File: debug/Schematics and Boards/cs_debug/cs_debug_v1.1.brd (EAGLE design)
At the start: 83.3 x 62.2 mm, 241 parts, among them J1 J-JTAG-CORTEX_SMD, J19 Solar, J2 J-JTAG-CORTEX_SMD, J3 J-JTAG-CORTEX-NEEDLE6-LEGS, J4 J-SERIAL-PORT, J5 J-WURTH-USBC, Q10 2N7002P, Q3 FDN340P, Q4 2N7002P, Q5 FDN340P, Q6 2N7002P, Q7 FDN340P, Q8 2N7002P, Q9 FDN340P, U1 AP2120N-3.3TRG1, U10 OPA357AIDBVTG4, U11 DAC7574IDGS, U12 MCP73871T-2CCI/ML, U13 USB2412-DZK, U14 INA225AIDGK, U15 OPA357AIDBVTG4, U2 TLV1117LV33DCYR, U5 INA225AIDGK, U6 OPA357AIDBVTG4, U7 INA225AIDGK, U8 OPA357AIDBVTG4, U9 INA225AIDGK, Y1 EPSON_TSX-3225_24.0000MF10Z-C3, Y101 32.768kHz, Y102 12mHz-12pF-K7

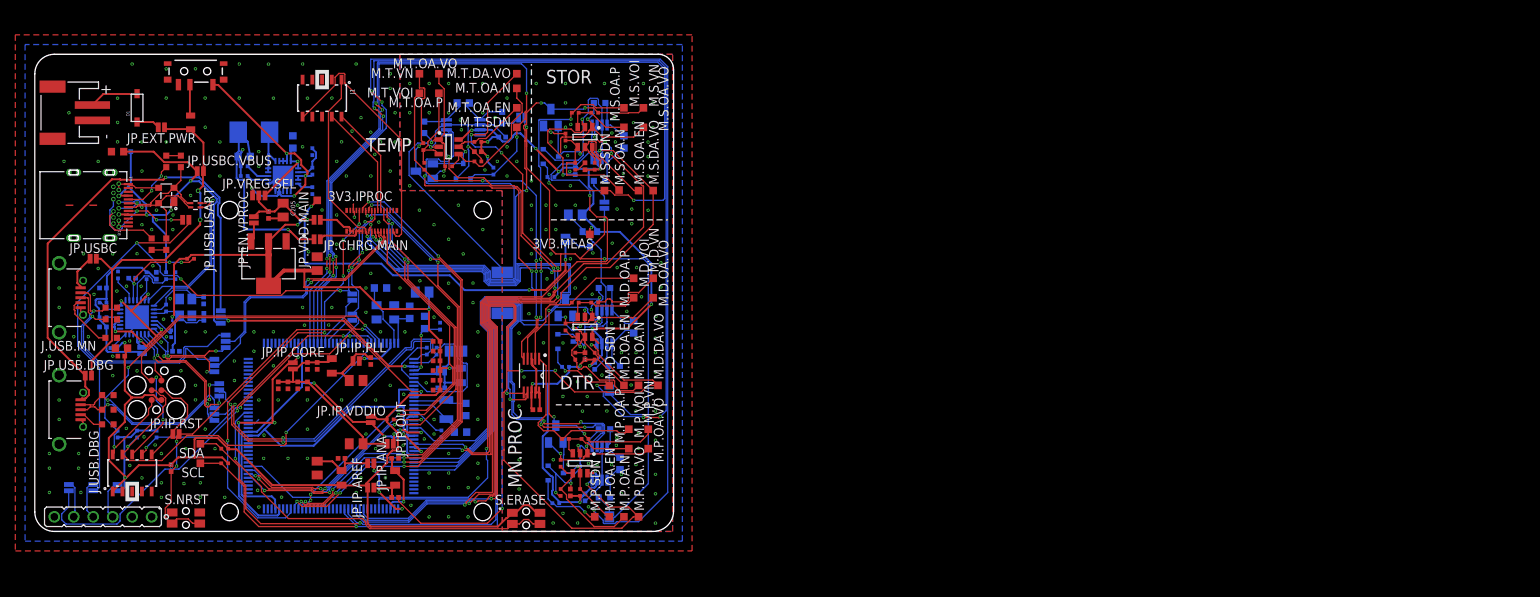
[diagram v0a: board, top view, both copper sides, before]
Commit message: Schematic updates and component placement for debug placement
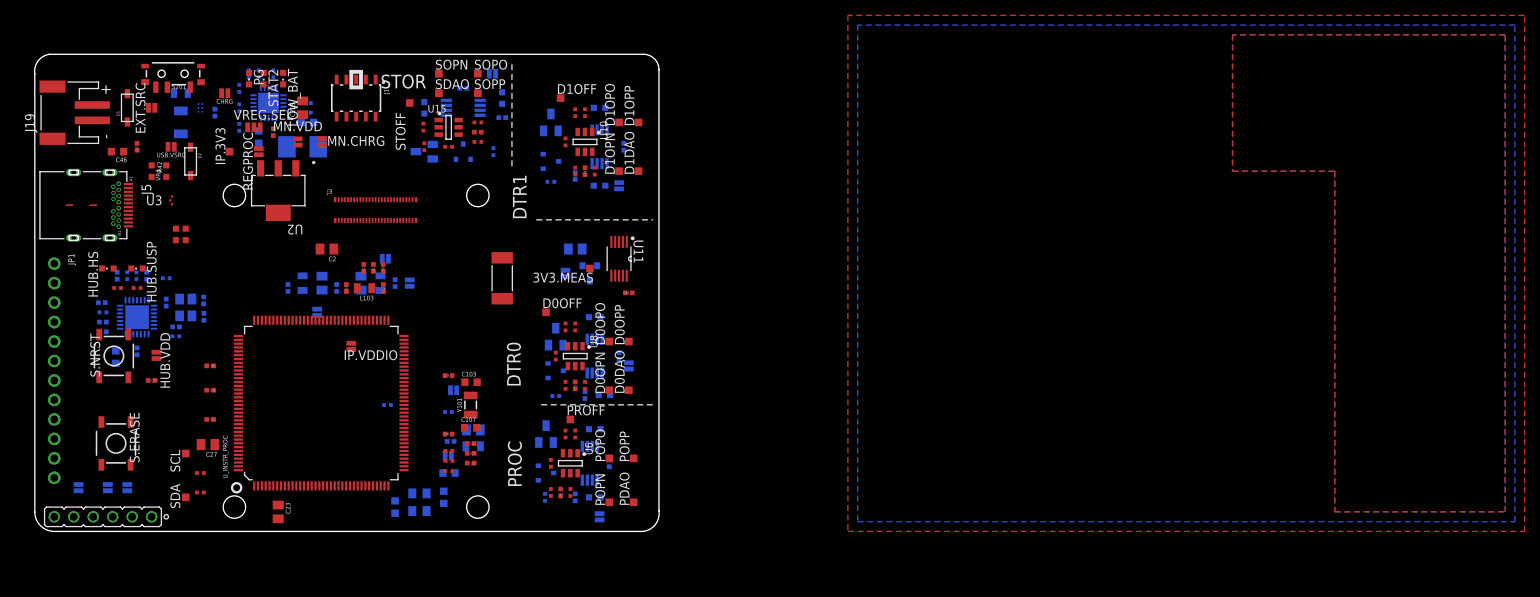
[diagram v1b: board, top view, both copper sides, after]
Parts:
- removed 3V3.IPROC, M.D.DA.VO, M.D.OA.EN, M.D.OA.N, M.D.OA.P, M.D.OA.VO, M.D.SDN, M.D.VN, M.D.VOI, M.P.DA.VO, M.P.OA.EN, M.P.OA.N, M.P.OA.P, M.P.OA.VO, M.P.SDN, M.P.VN, M.P.VOI, M.S.DA.VO, M.S.OA.EN, M.S.OA.N, M.S.OA.P, M.S.OA.VO, M.S.SDN, M.S.VN, M.S.VOI, M.T.DA.VO, M.T.OA.EN, M.T.OA.N, M.T.SDN, M.T.VN, M.T.VOI: TPTP10SQ, TestPoints:TP10SQ
- removed J.USB.DBG, J.USB.MN: USBABSMTDIP, ZX62D-AB-5P8:ZX62D-AB-5P8
- removed J2: J-JTAG-CORTEX_SMD, Connectors:SAMTECH_FTSH-105-01
- removed JP.CHRG.MAIN, JP.EN.VMEAS, JP.EN.VPROC, JP.EXT.PWR, JP.HUB.VDD, JP.IP.ANA, JP.IP.AREF, JP.IP.CORE, JP.IP.OUT, JP.IP.PLL, JP.IP.RST, JP.IP.UTMI, JP.IP.VDDIO, JP.P.DTR, JP.P.PROC, JP.P.STOR, JP.P.TEMP, JP.UART.RX, JP.UART.RX.IP, JP.UART.TX, JP.UART.TX.IP, JP.USB.USART, JP.USBC.VBUS, JP.VDD.MAIN: JUMPER-SMT_2_NC_PASTE_NO-SILK, Connectors:SMT-JUMPER_2_NC_PASTE_NO-SILK
- removed JP.USB.DBG, JP.USBC: JUMPER-SMT_2_NO_PASTEFREE, Connectors:SMT-JUMPER_2_NO_PASTEFREE_NO-SILK
- removed JP.USB.DDN, JP.USB.DDP, JP.USB.MDN, JP.USB.MDP, JP.USB.VBUSP, JP.VREG.SEL: JUMPER-SMT_3_1-NC_PASTE_NO-SILK, Connectors:SMT-JUMPER_3_1-NC_PASTE_NO-SILK
- removed J_DBG_TO_MAIN_HDR: HIROSE-DF40_30-PIN_CONNECTORS-HEADER, Connectors:HRS_DF40C-30DP-0.4V(51)
- removed L2: DLP11SN900HL2L, Inductors:IND_DLP11S_0504_MUR
- removed R44, R45, R51, R52: 10k, Resistors:R0402
- removed R50: 100k, Resistors:R0402
- removed VR1, VR2, VR5, VR6, VR7, VR8: VARISTOR, Diodes:R0603
- added C4, C5, C6: 0.1u, Capacitors:C0402
- added C57: 1u, Capacitors:C0402
- added CHRG, EXT.SRC, HUB.VDD, IP.ANA, IP.AREF, IP.OUT, IP.PLL, IP.UTMI, IP.VDDIO, MN.CHRG, MN.UART.RX, MN.UART.TX, MN.VDD, REGMEAS, REGPROC, USB.VSRC, VP.DTR0, VP.DTR1, VP.PRC, VP.STOR: JUMPER-SMT_2_NC_PASTE_NO-SILK, Connectors:SMT-JUMPER_2_NC_PASTE_NO-SILK
- added D0DAO, D0OFF, D0OPN, D0OPO, D0OPP, D1DAO, D1OFF, D1OPN, D1OPO, D1OPP, PDAO, POPN, POPO, POPP, PROFF, SOPO, SOPP, STOFF: TPSTP10SQ, TestPoints:TP10SQ
- added HUB.HS, HUB.SUSP, LOW_BAT, PG, STAT2: (no value), Diodes:CHIPLED_0603
- added IP.3V3: TPTP10SQ, TestPoints:TP10SQ
- added JP1: (no value), Connectors:1X12_ROUND
- added R10: 270, Resistors:R0402
- added R9: 750, Resistors:R0402
- added U204: LOADSWITCH-MIC94164, Switches:WLCSP6_2X3
- added U3: ESD122DMYR, Diodes:DMY0003A
- added VREG.SEL: JUMPER-SMT_3_1-NC_PASTE_NO-SILK, Connectors:SMT-JUMPER_3_1-NC_PASTE_NO-SILK
- C10, C13, C7: value 270nF -> 0.1u; device Capacitors:C0603 -> Capacitors:C0402
- C20: value 270nF -> 10u; device Capacitors:C0603 -> Capacitors:C1206
- D2: value BGX50A -> MBR120VLSFT3GOSCT-ND; device Diodes:SOT143_BGX50A -> adafruit:SOD-123
- J3: value J-JTAG-CORTEX-NEEDLE6-LEGS -> HIROSE-DF40_50-PIN_CONNECTORS-HEADER; device Connectors:8.06.16_6-PIN_NEEDLE_ADAPTER_LEGS -> Connectors:HRS_DF40C-50DP-0.4V(51)
- JP.UART.VCC: value JUMPER-SMT_2_NC_PASTE_NO-SILK -> JUMPER-SMT_2_NO_PASTEFREE; device Connectors:SMT-JUMPER_2_NC_PASTE_NO-SILK -> Connectors:SMT-JUMPER_2_NO_PASTEFREE_NO-SILK
- R2, R3: value 100k -> 1.5k
- R6: value 100k -> 1.15k
- R7: value 1M -> 100k
- S.ERASE, S.NRST: device Switches:SW_EVQ-P7L01P -> Switches:TACTILE_SWITCH_SMD_5.2MM
- SDAO, SOPN: value TPTP10SQ -> TPSTP10SQ
- Y102: value 12mHz-12pF-K7 -> 12MHz-12pF-K7
- moved S.ERASE 54.4 mm to (-12.3, 11.5), turned to 270 degrees
- moved R2 51.2 mm to (8.26, 59.7), turned to 90 degrees
- moved R3 49.6 mm to (6.35, 59.7), turned to 270 degrees
- moved R6 48.5 mm to (5.08, 59.7)
- moved C10 38.2 mm to (33.0, 57.8), turned to 180 degrees
- moved J3 37.0 mm to (21.6, 41.9), turned to 0 degrees
- moved C20 36.9 mm to (-3.81, 53.3), turned to 270 degrees
- moved C27 34.3 mm to (-0.28, 11.3), flipped to the top, turned to 180 degrees
- moved C17 28.6 mm to (24.1, 3.17), turned to 90 degrees
- moved C22 27.3 mm to (22.6, 31.8), turned to 90 degrees
- moved L101 25.9 mm to (22.2, 32.4), flipped to the bottom, turned to 270 degrees
- moved Y102 25.2 mm to (27.3, 3.81), turned to 270 degrees
- moved L103 25.1 mm to (20.1, 31.7), turned to 180 degrees
- moved C25 24.8 mm to (19.7, 32.4), flipped to the bottom, turned to 90 degrees
- moved C19 24.5 mm to (30.5, 4.45), turned to 270 degrees
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- renumbered M.T.OA.P to SDAO, M.T.OA.VO to SOPN
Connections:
- net CM_DIFFAMP_N2 renamed CM_DTR1_DIFFAMP_N
- net CM_DIFFAMP_P2 renamed CM_DTR1_DIFFAMP_P
- net CM_DTR_DIFFAMP_GAIN0 renamed CM_DTR0_DIFFAMP_GAIN0
- net CM_DTR_DIFFAMP_GAIN1 renamed CM_DTR0_DIFFAMP_GAIN1
- net CM_STORAGE_DIFFAMP_GAIN0 renamed CM_DTR1_DIFFAMP_GAIN0
- net CM_STORAGE_DIFFAMP_GAIN1 renamed CM_DTR1_DIFFAMP_GAIN1
- net CM_TEMP_DIFFAMP_GAIN0 renamed CM_STOR_DIFFAMP_GAIN0
- net CM_TEMP_DIFFAMP_GAIN1 renamed CM_STOR_DIFFAMP_GAIN1
- removed net CM_DIFFAMP_N1: C20.1, R58.2, U14.IN-
- removed net CM_DIFFAMP_N3: C10.1, R31.2, U7.IN-
- removed net CM_DIFFAMP_P1: C20.2, R59.2, U14.IN+
- removed net CM_DIFFAMP_P3: C10.2, R32.2, U7.IN+
- removed net CM_DTR_DCBIAS_SHUTDOWN: M.D.SDN.TP, Q8.G, R30.1, U_INSTR_PROC.15
- removed net CM_DTR_DIFFAMP_OUT: M.D.DA.VO.TP, U7.OUT, U_INSTR_PROC.82
- removed net CM_DTR_V_OFFSET_IN: M.D.VOI.TP, R25.1, U11.2
- removed net CM_DTR_V_SENSE_N: J_DBG_TO_MAIN_HDR.16, M.D.VN.TP, Q7.D, R26.1
- removed net CM_DTR_V_SENSE_P: JP.P.DTR.2, R32.1
- removed net CM_OPAMP_ENABLE1: M.T.OA.EN.TP, Q10.D, Q9.G, R54.1, U15.ENABLE
- removed net CM_OPAMP_ENABLE2: M.S.OA.EN.TP, Q5.G, Q6.D, R34.1, U10.ENABLE
- removed net CM_OPAMP_ENABLE3: M.D.OA.EN.TP, Q7.G, Q8.D, R27.1, U8.ENABLE
- removed net CM_OPAMP_N1: M.T.OA.N.TP, R55.1, R56.2, U15.IN-
- removed net CM_OPAMP_N2: M.S.OA.N.TP, R35.1, R36.2, U10.IN-
- removed net CM_OPAMP_N3: M.D.OA.N.TP, R28.1, R29.2, U8.IN-
- removed net CM_OPAMP_OUT1: Q9.S, R55.2, R58.1, SOPN.TP, U15.OUT
- removed net CM_OPAMP_OUT2: M.S.OA.VO.TP, Q5.S, R35.2, R38.1, U10.OUT
- removed net CM_OPAMP_OUT3: M.D.OA.VO.TP, Q7.S, R28.2, R31.1, U8.OUT
- removed net CM_OPAMP_P2: M.S.OA.P.TP, R24.2, R33.2, U10.IN+
- removed net CM_STORAGE_DCBIAS_SHUTDOWN: M.S.SDN.TP, Q6.G, R37.1, U_INSTR_PROC.14
- removed net CM_STORAGE_DIFFAMP_OUT: M.S.DA.VO.TP, U9.OUT, U_INSTR_PROC.83
- removed net CM_STORAGE_V_OFFSET_IN: M.S.VOI.TP, R24.1, U11.4
- removed net CM_STORAGE_V_SENSE_N: J_DBG_TO_MAIN_HDR.18, M.S.VN.TP, Q5.D, R33.1
- removed net CM_STORAGE_V_SENSE_P: JP.P.STOR.2, R39.1
- removed net CM_TEMP_DCBIAS_SHUTDOWN: M.T.SDN.TP, Q10.G, R57.1, U_INSTR_PROC.13
- removed net CM_TEMP_DIFFAMP_OUT: M.T.DA.VO.TP, U14.OUT, U_INSTR_PROC.84
- removed net CM_TEMP_V_OFFSET_IN: M.T.VOI.TP, R40.1, U11.5
- removed net CM_TEMP_V_SENSE_N: J_DBG_TO_MAIN_HDR.20, M.T.VN.TP, Q9.D, R53.1
- removed net CM_TEMP_V_SENSE_P: JP.P.TEMP.2, R59.1
- removed net HUB_INSTR_PROC_USB_D_N: JP.USB.DDN.3, U13.2
- removed net HUB_INSTR_PROC_USB_D_P: JP.USB.DDP.3, U13.3
- removed net HUB_MAIN_USB_DATA_N: JP.USB.MDN.3, U13.28
- removed net HUB_MAIN_USB_DATA_P: JP.USB.MDP.3, U13.1
- removed net INSTR_PROC_JTAG_TCK/SWCLK: J2.4, J3.4, R3.1, U_INSTR_PROC.28
- removed net INSTR_PROC_JTAG_TDI: J2.8, R6.1, U_INSTR_PROC.29
- removed net INSTR_PROC_JTAG_TDO/SWO: J2.6, J3.6, U_INSTR_PROC.30
- removed net INSTR_PROC_JTAG_TMS/SWDIO: J2.2, J3.2, R2.1, U_INSTR_PROC.31
- removed net INSTR_PROC_NRESET: J2.10, J3.3, JP.IP.RST.1
- removed net MAIN_TRACE_CLK/GPIO4: J_DBG_TO_MAIN_HDR.26, U_INSTR_PROC.97
- removed net MAIN_TRACE_D0/GPIO6: J_DBG_TO_MAIN_HDR.23, U_INSTR_PROC.114
- removed net MAIN_TRACE_D1/GPIO7: J_DBG_TO_MAIN_HDR.25, U_INSTR_PROC.115
- removed net MAIN_TRACE_D2/GPIO8: J_DBG_TO_MAIN_HDR.27
- removed net MAIN_TRACE_D3/GPIO9: J_DBG_TO_MAIN_HDR.29
- removed net MAIN_TRACE_SWO/GPIO5: J_DBG_TO_MAIN_HDR.28, U_INSTR_PROC.113
- removed net USB_BKUP_DBG_D_N: J.USB.DBG.D-, JP.USB.DDN.1, VR5.1
- removed net USB_BKUP_DBG_D_P: J.USB.DBG.D+, JP.USB.DDP.1, VR2.1
- removed net USB_BKUP_DBG_OTGID: J.USB.DBG.USBID, VR1.1
- removed net USB_BKUP_DBG_VBUS: J.USB.DBG.VBUS, JP.USB.DBG.2, JP.USB.VBUSP.1
- removed net USB_BKUP_MAIN_D_N: J.USB.MN.D-, JP.USB.MDP.1, VR8.1
- removed net USB_BKUP_MAIN_D_P: J.USB.MN.D+, JP.USB.MDN.1, VR7.1
- removed net USB_BKUP_MAIN_OTGID: J.USB.MN.USBID, VR6.1
- removed net USB_BKUP_MAIN_VBUS: J.USB.MN.VBUS, JP.USBC.2
- removed net USB_CONN_D_N: D2.2, J5.A6, J5.B6, L2.3, VR3.1
- removed net USB_CONN_D_P: D2.4, J5.A7, J5.B7, L2.2, VR4.1
- removed net VDDOUT_1: JP.IP.CORE.1, U_INSTR_PROC.10, U_INSTR_PROC.104, U_INSTR_PROC.124, U_INSTR_PROC.45, U_INSTR_PROC.61
- new net +3V3_INSTR_PROC: HUB.VDD.1
- new net CM_DTR0_DCBIAS_SHUTDOWN: Q8.G, R30.1, U_INSTR_PROC.15
- new net CM_DTR0_DIFFAMP_N: C7.1, R31.2, U7.IN-
- new net CM_DTR0_DIFFAMP_OUT: D0DAO.TP, U7.OUT, U_INSTR_PROC.82
- new net CM_DTR0_DIFFAMP_P3: C7.2, R32.2, U7.IN+
- new net CM_DTR0_OPAMP_ENABLE: Q7.G, Q8.D, R27.1, U8.ENABLE
- new net CM_DTR0_OPAMP_N: D0OPN.TP, R28.1, R29.2, U8.IN-
- new net CM_DTR0_OPAMP_OUT: D0OPO.TP, Q7.S, R28.2, R31.1, U8.OUT
- new net CM_DTR0_V_OFFSET_IN: D0OFF.TP, R25.1, U11.2
- new net CM_DTR0_V_SENSE_N: J3.18, Q7.D, R26.1
- new net CM_DTR0_V_SENSE_P: R32.1, VP.DTR0.2
- new net CM_DTR1_DCBIAS_SHUTDOWN: Q6.G, R37.1, U_INSTR_PROC.14
- new net CM_DTR1_DIFFAMP_OUT: D1DAO.TP, U9.OUT, U_INSTR_PROC.83
- new net CM_DTR1_OPAMP_N: D1OPN.TP, R35.1, R36.2, U10.IN-
- new net CM_DTR1_OPAMP_OUT: D1OPO.TP, Q5.S, R35.2, R38.1, U10.OUT
- new net CM_DTR1_OPAMP_P: D1OPP.TP, R24.2, R33.2, U10.IN+
- new net CM_DTR1_V_OFFSET_IN: D1OFF.TP, R24.1, U11.4
- new net CM_DTR1_V_SENSE_N: J3.20, Q5.D, R33.1
- new net CM_DTR1_V_SENSE_P: R39.1, VP.DTR1.2
- new net CM_DTR_OPAMP_ENABLE: Q5.G, Q6.D, R34.1, U10.ENABLE
- new net CM_STORV_SENSE_N: J3.22
- new net CM_STOR_DCBIAS_SHUTDOWN: Q10.G, R57.1, U_INSTR_PROC.13
- new net CM_STOR_DIFFAMP_N1: C10.1, R58.2, U14.IN-
- new net CM_STOR_DIFFAMP_OUT: SDAO.TP, U14.OUT, U_INSTR_PROC.84
- new net CM_STOR_DIFFAMP_P1: C10.2, R59.2, U14.IN+
- new net CM_STOR_OPAMP_ENABLE: Q10.D, Q9.G, R54.1, U15.ENABLE
- new net CM_STOR_OPAMP_N: R55.1, R56.2, SOPN.TP, U15.IN-
- new net CM_STOR_OPAMP_OUT: Q9.S, R55.2, R58.1, SOPO.TP, U15.OUT
- new net CM_STOR_V_OFFSET_IN: R40.1, STOFF.TP, U11.5
- new net CM_STOR_V_SENSE_N: Q9.D, R53.1
- new net CM_STOR_V_SENSE_P: R59.1, VP.STOR.2
- new net MAIN_GPIO10: J3.40, U_INSTR_PROC.114
- new net MAIN_GPIO11: J3.38, U_INSTR_PROC.115
- new net MAIN_GPIO4/SERCOM_P0: J3.30, JP1.2
- new net MAIN_GPIO5/SERCOM_P1: J3.32, JP1.3
- new net MAIN_GPIO6/SERCOM_P2: J3.34, JP1.4
- new net MAIN_GPIO7/SERCOM_P3: J3.36, JP1.5
- new net MAIN_GPIO8: J3.44, U_INSTR_PROC.97
- new net MAIN_GPIO9: J3.42, U_INSTR_PROC.113
- new net MAIN_TRACE_CLK/GPIO17: J3.23, JP1.11
- new net MAIN_TRACE_D0/GPIO13: J3.15, JP1.7
- new net MAIN_TRACE_D1/GPIO14: J3.17, JP1.8
- new net MAIN_TRACE_D2/GPIO15: J3.19, JP1.9
- new net MAIN_TRACE_D3/GPIO16: J3.21, JP1.10
- new net MAIN_TRACE_SWO/GPIO12: J3.13, JP1.6
- new net N$12: R2.1, U12.8
- new net N$17: C5.1, U13.25
- new net N$18: R3.2, STAT2.C
- new net N$19: PG.C, R6.2
- new net N$20: R6.1, U12.6
- new net N$22: HUB.SUSP.A, R9.1
- new net N$23: HUB.HS.A, R10.1
- new net N$24: CHRG.1, R201.2, U12.17, U12.18, U12.19, U12.3, U12.4, U12.9
- new net VUSB_DIODE: D2.C, USB.VSRC.1
- net 3V3_INSTR_MEAS: now also JP1.1
- net 3V3_INSTR_PROC: now also IP.3V3.TP, IP.AREF.1, IP.VDDIO.2, S.ERASE.1; no longer 3V3.IPROC.TP, C49.1, C50.1, C51.1, C52.1, C53.1, C54.1, J2.1, J3.1, JP.HUB.VDD.1, JP.IP.AREF.1, JP.IP.VDDIO.2, R2.2, R3.2, R44.2, R45.2, R51.2, R52.2, R6.2, S.ERASE.1_1, S.ERASE.1_2
- net ADVREF_PRE: now also IP.AREF.2; no longer JP.IP.AREF.2
- net CM_DIFFAMP_N4: now also C6.1; no longer C7.1
- net CM_DIFFAMP_P4: now also C6.2; no longer C7.2
- net CM_OPAMP_ENABLE4: no longer M.P.OA.EN.TP
- net CM_OPAMP_N4: now also POPN.TP; no longer M.P.OA.N.TP
- net CM_OPAMP_OUT4: now also POPO.TP; no longer M.P.OA.VO.TP
- net CM_OPAMP_P1: now also SOPP.TP; no longer SDAO.TP
- net CM_OPAMP_P3: now also D0OPP.TP; no longer M.D.OA.P.TP
- net CM_OPAMP_P4: now also POPP.TP; no longer M.P.OA.P.TP
- net CM_PROC_DCBIAS_SHUTDOWN: no longer M.P.SDN.TP
- net CM_PROC_DIFFAMP_OUT: now also PDAO.TP; no longer M.P.DA.VO.TP
- net CM_PROC_V_OFFSET_IN: now also PROFF.TP; no longer M.P.VOI.TP
- net CM_PROC_V_SENSE_N: now also J3.16; no longer J_DBG_TO_MAIN_HDR.14, M.P.VN.TP
- net CM_PROC_V_SENSE_P: now also VP.PRC.2; no longer JP.P.PROC.2
- net DGND: now also C20.2, C4.2, C5.2, C57.2, HUB.HS.C, HUB.SUSP.C, J3.1, J3.3, J3.7, JP1.12, R7.1, S.NRST.1, U204.C1, U3.1; no longer D2.3, J.USB.DBG.GND, J.USB.DBG.S1, J.USB.DBG.S2, J.USB.DBG.S3, J.USB.DBG.S4, J.USB.MN.GND, J.USB.MN.S1, J.USB.MN.S2, J.USB.MN.S3, J.USB.MN.S4, J2.3, J2.5, J2.9, J_DBG_TO_MAIN_HDR.1, J_DBG_TO_MAIN_HDR.3, J_DBG_TO_MAIN_HDR.5, R50.1, S.NRST.1_1, S.NRST.1_2, VR1.2, VR2.2, VR5.2, VR6.2, VR7.2, VR8.2
- net ERASE_S: now also S.ERASE.3; no longer S.ERASE.2_1, S.ERASE.2_2
- net INSTR_PROC_NRESET_SW: now also S.NRST.3; no longer JP.IP.RST.2, S.NRST.2_1, S.NRST.2_2
- net INSTR_PROC_USB_D_N: now also U13.28; no longer JP.USB.DDN.2
- net INSTR_PROC_USB_D_P: now also U13.1; no longer JP.USB.DDP.2
- net MAIN_GPIO0: now also J3.31; no longer J_DBG_TO_MAIN_HDR.7
- net MAIN_GPIO1: now also J3.29; no longer J_DBG_TO_MAIN_HDR.9
- net MAIN_GPIO2: now also J3.27; no longer J_DBG_TO_MAIN_HDR.11
- net MAIN_GPIO3: now also J3.25; no longer J_DBG_TO_MAIN_HDR.13
- net MAIN_NRESET: now also J3.24; no longer J_DBG_TO_MAIN_HDR.30
- net MAIN_SWD_SWCLK: now also J3.28; no longer J_DBG_TO_MAIN_HDR.19
- net MAIN_SWD_SWDIO: now also J3.26; no longer J_DBG_TO_MAIN_HDR.21
- net MAIN_USART_RX: now also J3.9, MN.UART.RX.1; no longer JP.UART.RX.1, JP.UART.TX.IP.1, J_DBG_TO_MAIN_HDR.17
- net MAIN_USART_TX: now also J3.11, MN.UART.TX.1; no longer JP.UART.RX.IP.1, JP.UART.TX.1, JP.USB.USART.2, J_DBG_TO_MAIN_HDR.15
- net MAIN_USB_DATA_N: now also J3.49, U13.2; no longer JP.USB.MDN.2, J_DBG_TO_MAIN_HDR.22
- net MAIN_USB_DATA_P: now also J3.47, U13.3; no longer JP.USB.MDP.2, J_DBG_TO_MAIN_HDR.24
- net N$1: now also REGMEAS.2; no longer JP.EN.VMEAS.2
- net N$14: now also R3.1, U12.7; no longer R45.1, U13.7
- net N$15: now also EXT.SRC.1; no longer JP.EXT.PWR.1
- net N$16: now also C4.1, U13.9; no longer R44.1, U13.11
- net N$3: now also S201.2, U204.C2; no longer JP.UART.TX.IP.2, U_INSTR_PROC.18
- net N$4: now also REGPROC.2; no longer JP.EN.VPROC.2
- net N$5: now also LOW_BAT.C, R2.2; no longer JP.UART.RX.IP.2, U_INSTR_PROC.17
- net N$6: now also C20.1, S201.3, U204.A2, U204.B2; no longer S201.2
- net N$7: now also MN.UART.TX.2; no longer JP.UART.TX.2
- net N$9: now also MN.UART.RX.2; no longer JP.UART.RX.2
- net UCTX_DBGRX: no longer JP.USB.USART.1
- net USBC_VBUS: now also D2.A; no longer D2.1, JP.USB.VBUSP.3, JP.USBC.VBUS.1
- net USB_D_N: now also J5.A7, J5.B7, U3.2, VR3.1; no longer L2.4
- net USB_D_P: now also J5.A6, J5.B6, U3.3, VR4.1; no longer L2.1
- net USB_HS_IND: now also R10.2; no longer R50.2
- net USB_HUB_VDD: now also C49.1, C50.1, C51.1, C52.1, C53.1, C54.1, HUB.VDD.2; no longer JP.HUB.VDD.2
- net USB_NONRMV0: now also R9.2; no longer R51.1
- net USB_NONRMV1: now also R7.2; no longer R52.1
- net USB_VBUS_IPROC: no longer JP.USB.VBUSP.2
- net USB_XIN: no longer R7.2
- net USB_XOUT: no longer R7.1
- net VCHRG_BATT: now also MN.CHRG.1; no longer JP.CHRG.MAIN.1
- net VCHRG_OUT: now also VREG.SEL.3; no longer JP.VREG.SEL.3
- net VDDANA1: now also IP.ANA.2; no longer JP.IP.ANA.2
- net VDDANA_0: now also IP.ANA.1; no longer JP.IP.ANA.1
- net VDDIO1: now also IP.VDDIO.1; no longer JP.IP.VDDIO.1
- net VDDOUT: now also IP.OUT.2, U_INSTR_PROC.10, U_INSTR_PROC.104, U_INSTR_PROC.124, U_INSTR_PROC.45, U_INSTR_PROC.61; no longer JP.IP.CORE.2, JP.IP.OUT.2
- net VDDOUTMI: now also IP.UTMI.2; no longer JP.IP.UTMI.2
- net VDDOUTMI_0: now also IP.UTMI.1; no longer JP.IP.UTMI.1
- net VDDOUT_0: now also IP.OUT.1; no longer JP.IP.OUT.1
- net VDDPLL: now also IP.PLL.2; no longer JP.IP.PLL.2
- net VDDPLL_0: now also IP.PLL.1; no longer JP.IP.PLL.1
- net VDD_TO_MAIN: now also J3.2, J3.4, J3.6, MN.VDD.2; no longer JP.VDD.MAIN.2, J_DBG_TO_MAIN_HDR.2, J_DBG_TO_MAIN_HDR.4
- net VREG_IN: now also MN.VDD.1, REGMEAS.1, REGPROC.1, VREG.SEL.2; no longer JP.EN.VMEAS.1, JP.EN.VPROC.1, JP.VDD.MAIN.1, JP.VREG.SEL.2
- net VSRC: now also EXT.SRC.2, USB.VSRC.2; no longer JP.EXT.PWR.2, JP.USB.DBG.1, JP.USBC.1, JP.USBC.VBUS.2
- net VSRC_RAW: now also C57.1, CHRG.2, LOW_BAT.A, PG.A, STAT2.A, U204.A1, U204.B1, VREG.SEL.1; no longer JP.VREG.SEL.1, R201.2, S201.3, U12.17, U12.18, U12.19, U12.3, U12.4, U12.9
- net V_BATT_MAIN: now also J3.10, J3.12, J3.8, MN.CHRG.2; no longer JP.CHRG.MAIN.2, J_DBG_TO_MAIN_HDR.10, J_DBG_TO_MAIN_HDR.6, J_DBG_TO_MAIN_HDR.8
- net V_SENSE_P: now also J3.14, VP.DTR0.1, VP.DTR1.1, VP.PRC.1, VP.STOR.1; no longer JP.P.DTR.1, JP.P.PROC.1, JP.P.STOR.1, JP.P.TEMP.1, J_DBG_TO_MAIN_HDR.12
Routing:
- net 3V3_INSTR_PROC: track 245.0 -> 0.00 mm, vias 7 -> 0
- net AGND: track 160.7 -> 0.00 mm, vias 127 -> 0
- net CM_PROC_DCBIAS_SHUTDOWN: track 159.5 -> 0.00 mm, vias 6 -> 0
- net CM_DTR_DCBIAS_SHUTDOWN: track 147.7 -> 0.00 mm, vias 8 -> 0
- net V_SENSE_P: track 140.3 -> 0.00 mm, vias 5 -> 0
- net 3V3_INSTR_MEAS: track 123.0 -> 0.00 mm, vias 14 -> 0
- net CM_STORAGE_DCBIAS_SHUTDOWN: track 114.7 -> 0.00 mm, vias 6 -> 0
- net CM_DTR1_DIFFAMP_GAIN0: track 103.0 -> 0.00 mm, vias 2 -> 0
- net CM_PROC_DIFFAMP_OUT: track 97.1 -> 0.00 mm, vias 2 -> 0
- net INSTR_PROC_I2C_SDA: track 96.4 -> 0.00 mm, vias 2 -> 0
- net CM_TEMP_DIFFAMP_OUT: track 95.8 -> 0.00 mm, vias 5 -> 0
- net INSTR_PROC_I2C_SCL: track 93.3 -> 0.00 mm, vias 2 -> 0
- net CM_DTR_DIFFAMP_OUT: track 90.7 -> 0.00 mm, vias 4 -> 0
- net MAIN_USART_TX: track 89.2 -> 0.00 mm, vias 6 -> 0
- net CM_STORAGE_DIFFAMP_OUT: track 87.0 -> 0.00 mm, vias 2 -> 0
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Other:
- board size 83.3 x 62.2 mm -> 81.5 x 62.2 mm
- board text added: "DTR0"
- board text added: "DTR1"
- board text added: "PROC"
- board text removed: "DTR"
- board text removed: "MN.PROC"
- board text removed: "TEMP"

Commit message: Finished schematic revision for main, debug boards.
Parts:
- C.PHAT: value 10u -> 47u
- moved IP.VDDIO 13.7 mm to (6.99, 31.8), flipped to the bottom, turned to 90 degrees
- moved C2 11.9 mm to (3.81, 40.0), turned to 270 degrees
- moved R41 7.97 mm to (31.1, 16.0), flipped to the top, turned to 0 degrees
- moved D1OFF 1.91 mm to (43.8, 56.5)
- moved STOFF 1.91 mm to (26.0, 54.0)
- moved SDAO 1.90 mm to (27.9, 57.1)
- moved SOPN 1.90 mm to (27.9, 59.7)
- moved C16 1.27 mm to (55.9, 31.1)
- moved D0OPO 1.27 mm to (52.1, 26.0)
- moved D0OPP 1.27 mm to (54.6, 26.0)
- moved POPO 1.27 mm to (52.1, 10.8)
- moved POPP 1.27 mm to (55.2, 10.8)
- moved D1OPO 1.27 mm to (53.3, 54.6)
- moved D1OPP 1.27 mm to (55.9, 54.6)
- moved IP.PLL 0.90 mm to (14.6, 29.2)
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- renumbered C20 to C.PHAT, J4 to J.FTDI, R1 to R.GND, U_INSTR_PROC to U.IP
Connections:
- net N$3 renamed VREG.SW.EN
- net N$6 renamed VSRC_SW
- removed net USB_VBUS_IPROC: U.IP.39
- net USBC_VBUS: now also U.IP.39
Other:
- board text added: "GPIO_MAIN"

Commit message: Route differential USB signals
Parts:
- added R1: 51k, Resistors:R0402
- moved VR4 5.72 mm to (-2.54, 44.5), turned to 0 degrees
- moved VR3 5.46 mm to (-2.54, 42.5), turned to 0 degrees
- moved C39 1.19 mm to (34.0, 7.72)
- moved C37 0.99 mm to (34.0, 9.19)
- moved C38 0.92 mm to (34.0, 10.5)
- moved C52 0.36 mm to (-5.66, 30.2)
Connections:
- removed net N$22: HUB.SUSP.A, R9.1
- new net N$3: HUB.SUSP.C, R9.1
- net 3V3_INSTR_PROC: now also HUB.SUSP.A, R1.1
- net DGND: no longer HUB.SUSP.C
- net USB_NONRMV0: now also R1.2
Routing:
- net MAIN_USB_DATA_N: track 0.00 -> 58.5 mm, vias 0 -> 3
- net MAIN_USB_DATA_P: track 0.00 -> 58.3 mm, vias 0 -> 3
- net INSTR_PROC_USB_D_P: track 0.00 -> 54.1 mm, vias 0 -> 1
- net INSTR_PROC_USB_D_N: track 0.00 -> 53.6 mm, vias 0 -> 1
- net USB_D_P: track 0.00 -> 30.9 mm, vias 0 -> 2
- net USB_D_N: track 0.00 -> 27.8 mm, vias 0 -> 2
- net USB_XOUT: track 0.00 -> 8.94 mm
- net USB_XIN: track 0.00 -> 7.15 mm

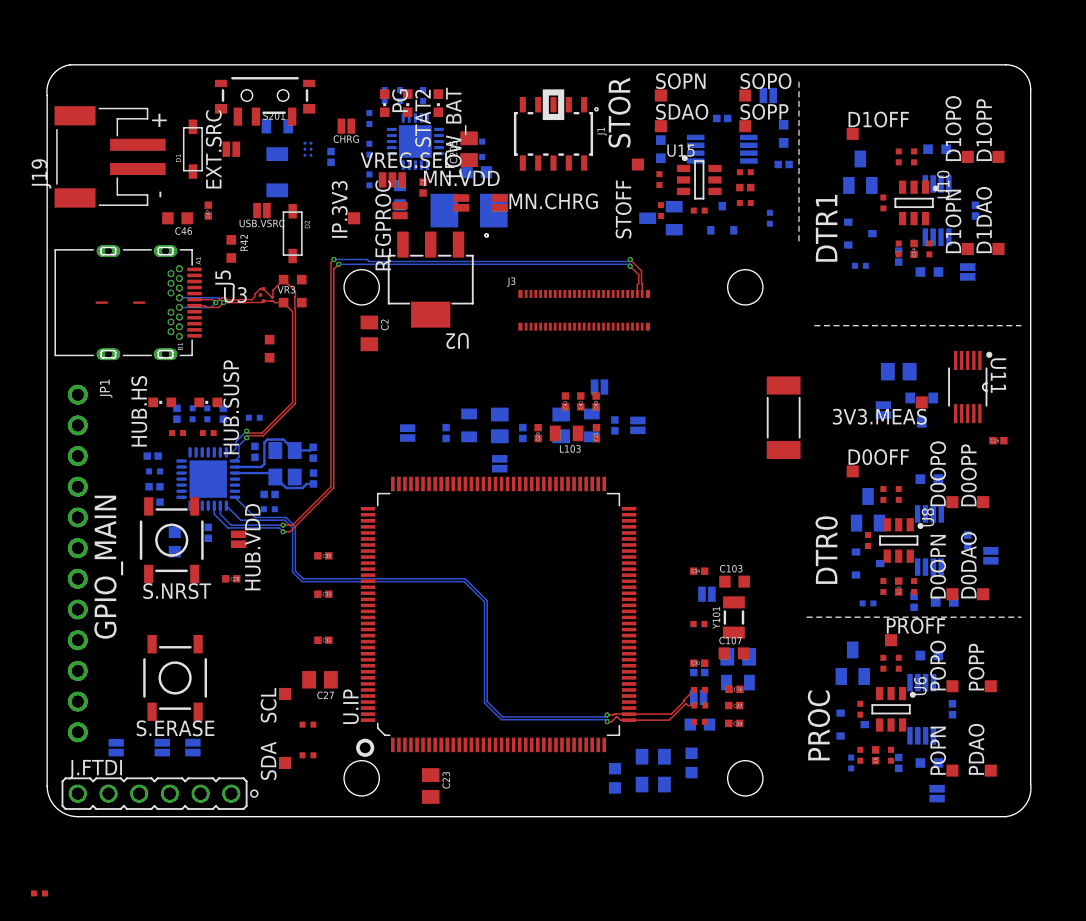
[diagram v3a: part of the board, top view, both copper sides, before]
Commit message: Edit silk and documentation layers for pick-and-place assembly
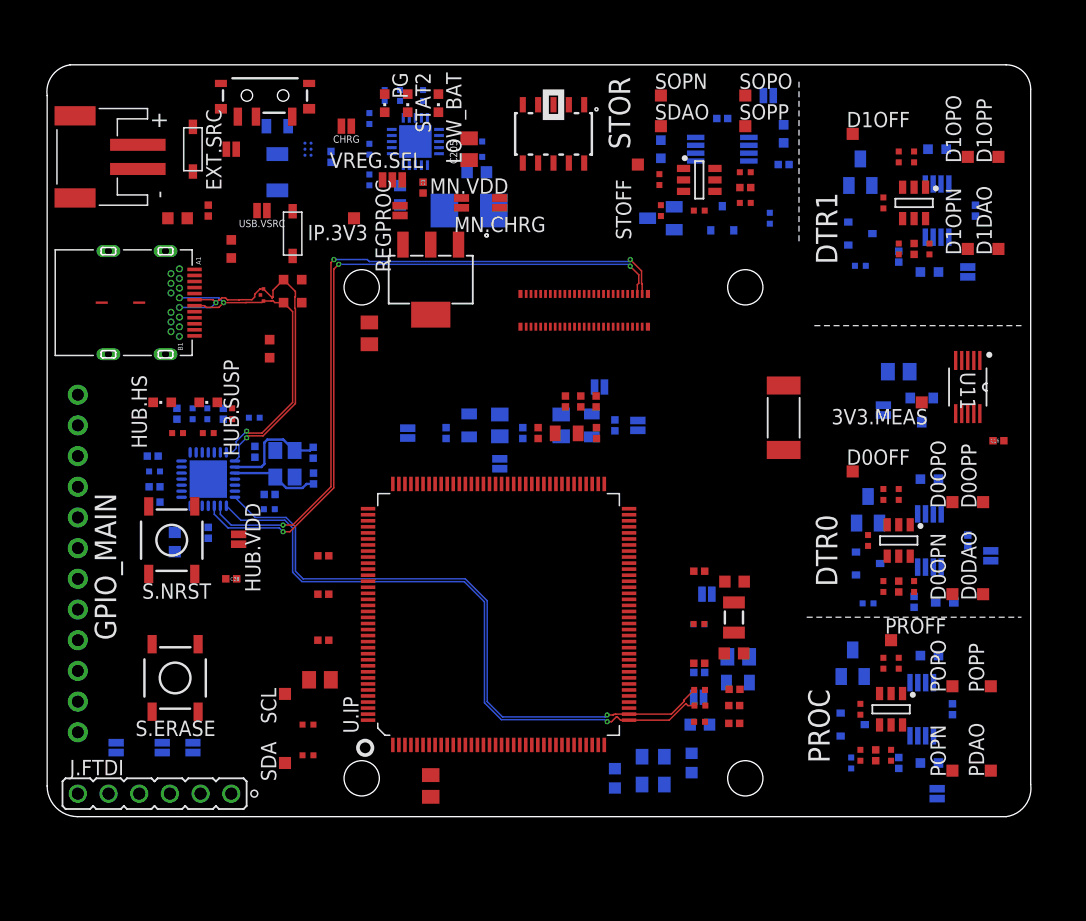
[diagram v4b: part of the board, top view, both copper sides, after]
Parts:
- moved R1 42.8 mm to (-7.54, 33.4), turned to 270 degrees
- renumbered JP.UART.VCC to UART.VCC

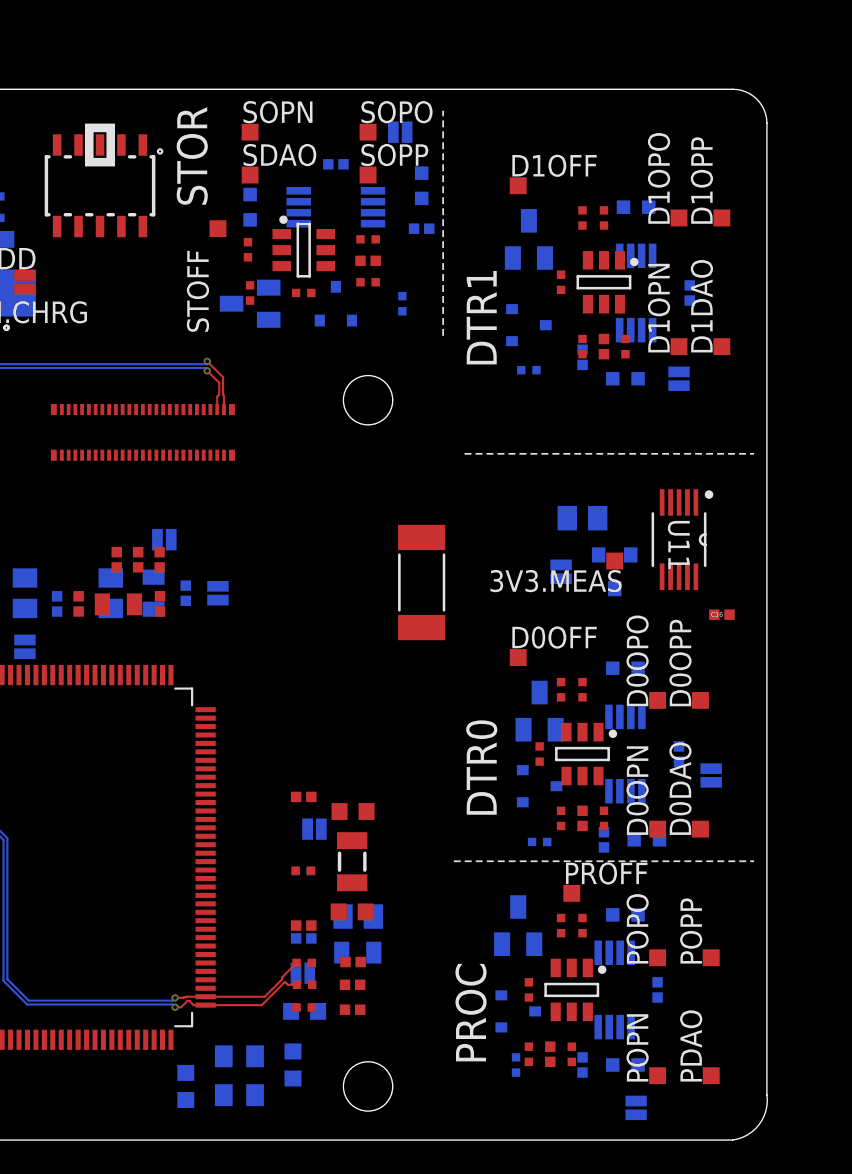
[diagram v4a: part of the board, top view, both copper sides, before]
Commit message: Route minimal analog signals under ground bridge, add near ground plugs
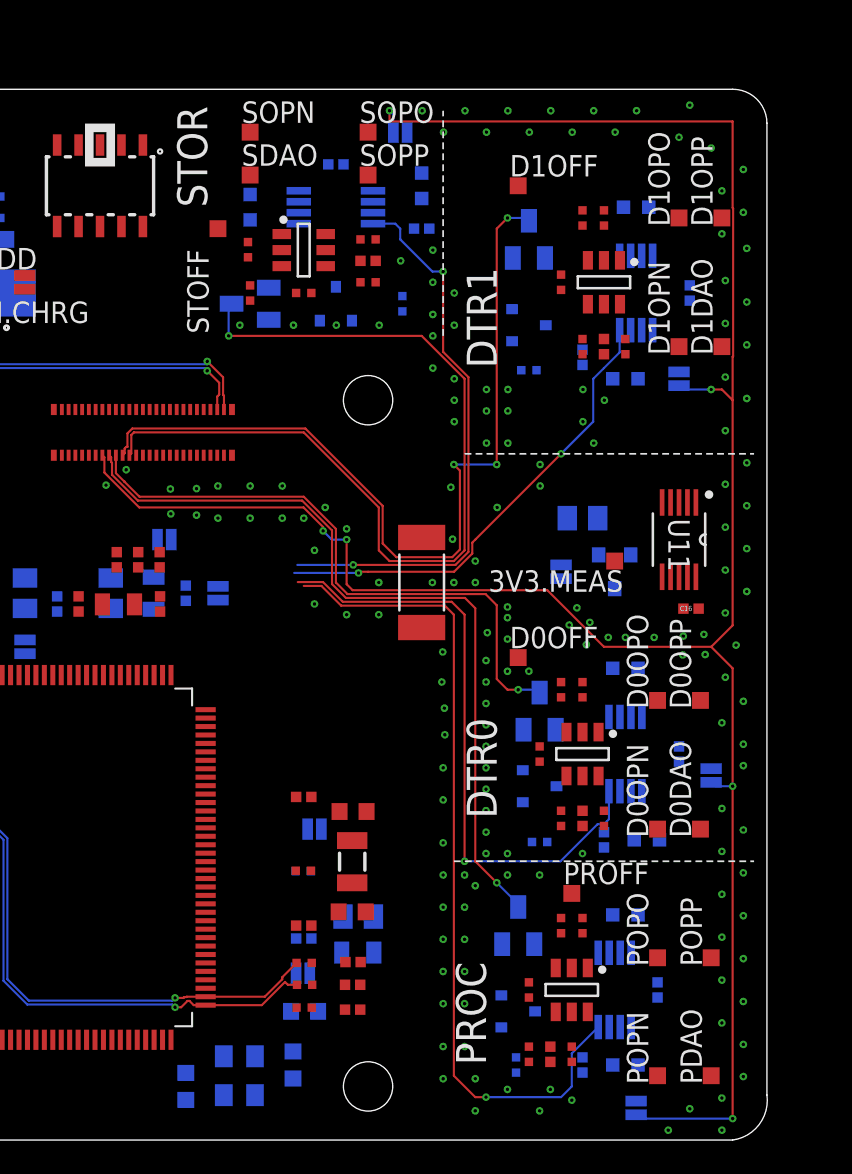
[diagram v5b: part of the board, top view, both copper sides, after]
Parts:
- moved C16 1.86 mm to (54.1, 31.5)
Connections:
- removed net CM_STORV_SENSE_N: J3.22
- net CM_STOR_V_SENSE_N: now also J3.22
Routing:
- net V_SENSE_P: track 0.00 -> 136.1 mm, vias 0 -> 6
- net CM_STOR_V_SENSE_N: track 0.00 -> 53.1 mm, vias 0 -> 1
- net CM_DTR1_V_SENSE_N: track 0.00 -> 49.8 mm, vias 0 -> 3
- net CM_PROC_DIFFAMP_OUT: track 0.00 -> 48.8 mm, vias 0 -> 1
- net CM_PROC_V_SENSE_N: track 0.00 -> 46.6 mm, vias 0 -> 1
- net CM_DTR0_DIFFAMP_OUT: track 0.00 -> 36.5 mm, vias 0 -> 1
- net CM_DTR0_V_SENSE_N: track 0.00 -> 36.0 mm, vias 0 -> 1
- net CM_STOR_DIFFAMP_OUT: track 0.00 -> 33.4 mm, vias 0 -> 2
- net CM_DTR1_DIFFAMP_OUT: track 0.00 -> 27.9 mm, vias 0 -> 2
